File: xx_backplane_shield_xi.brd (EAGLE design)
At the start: 80 x 82.5 mm, 25 parts

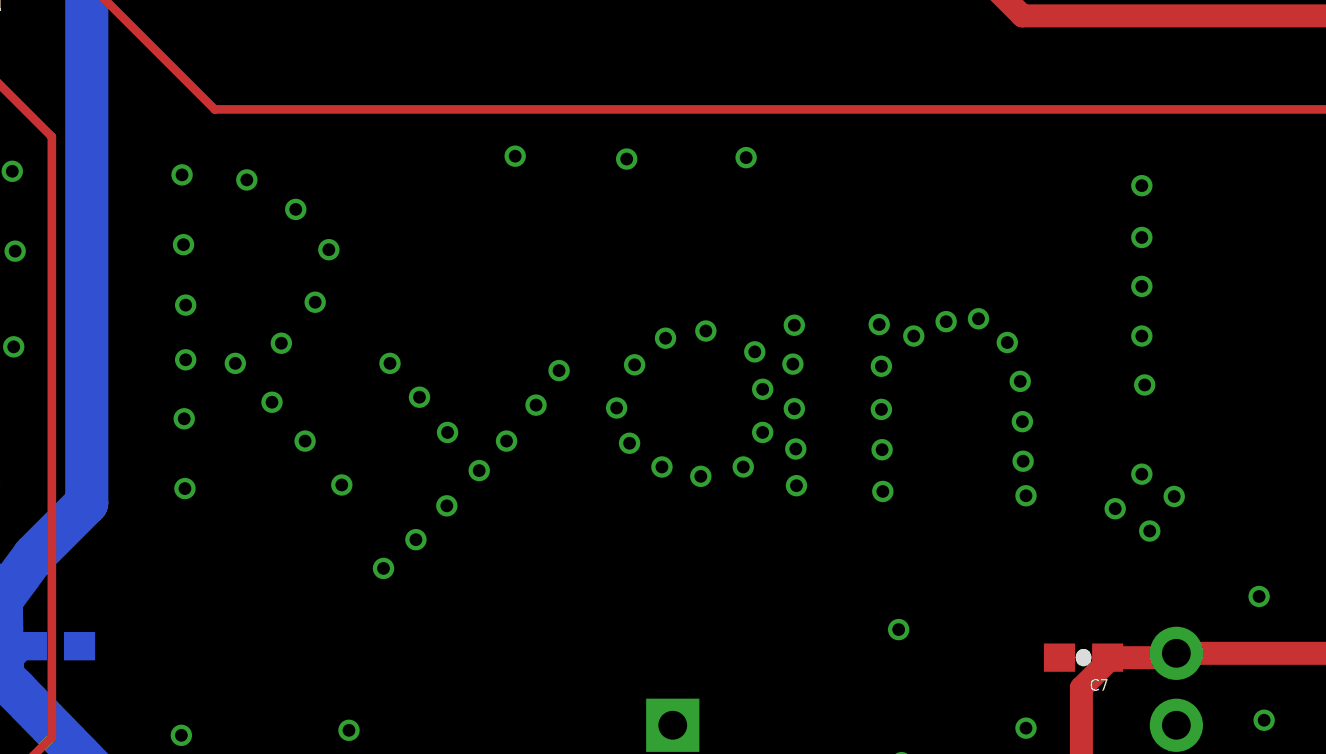
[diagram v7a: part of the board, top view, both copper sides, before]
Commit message: removing a few vias from my name
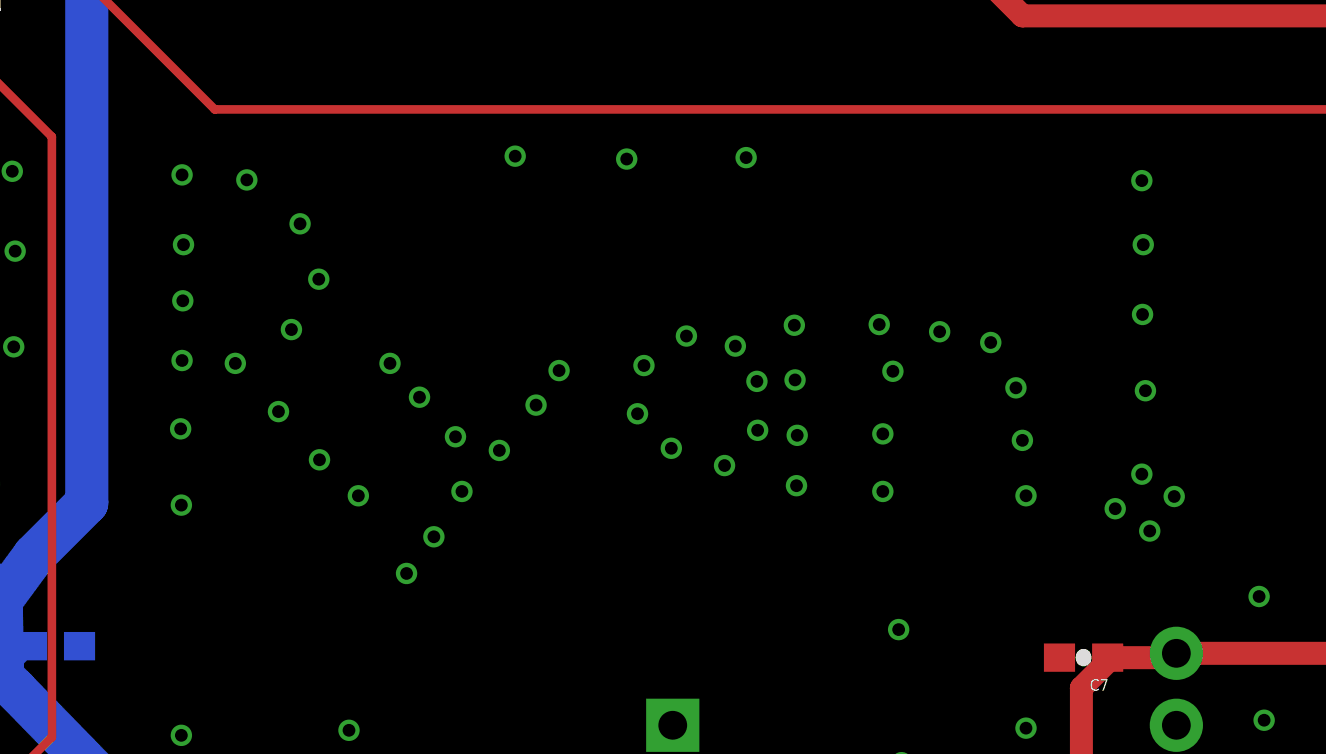
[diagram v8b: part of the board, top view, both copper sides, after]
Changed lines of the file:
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@@
 <via x="5.1562" y="56.4388" extent="1-16" drill="0.45"/>
 <via x="5.207" y="53.975" extent="1-16" drill="0.45"/>
-<via x="5.2832" y="51.8414" extent="1-16" drill="0.45"/>
-<via x="5.2832" y="49.911" extent="1-16" drill="0.45"/>
-<via x="5.2324" y="47.8282" extent="1-16" drill="0.45"/>
-<via x="5.2578" y="45.3644" extent="1-16" drill="0.45"/>
+<via x="5.1816" y="51.9938" extent="1-16" drill="0.45"/>
+<via x="5.1562" y="49.8856" extent="1-16" drill="0.45"/>
+<via x="5.1054" y="47.4726" extent="1-16" drill="0.45"/>
+<via x="5.1308" y="44.7802" extent="1-16" drill="0.45"/>
 <via x="7.4422" y="56.261" extent="1-16" drill="0.45"/>
-<via x="9.1694" y="55.2196" extent="1-16" drill="0.45"/>
-<via x="10.3378" y="53.7972" extent="1-16" drill="0.45"/>
-<via x="9.8552" y="51.943" extent="1-16" drill="0.45"/>
-<via x="8.6614" y="50.4952" extent="1-16" drill="0.45"/>
+<via x="9.3218" y="54.7116" extent="1-16" drill="0.45"/>
+<via x="9.9822" y="52.7558" extent="1-16" drill="0.45"/>
+<via x="9.017" y="50.9778" extent="1-16" drill="0.45"/>
 <via x="7.0358" y="49.784" extent="1-16" drill="0.45"/>
-<via x="8.3312" y="48.4124" extent="1-16" drill="0.45"/>
-<via x="9.4996" y="47.0408" extent="1-16" drill="0.45"/>
-<via x="10.795" y="45.4914" extent="1-16" drill="0.45"/>
+<via x="8.5598" y="48.0822" extent="1-16" drill="0.45"/>
+<via x="10.0076" y="46.3804" extent="1-16" drill="0.45"/>
+<via x="11.3792" y="45.1104" extent="1-16" drill="0.45"/>
 <via x="12.4968" y="49.784" extent="1-16" drill="0.45"/>
 <via x="13.5382" y="48.5902" extent="1-16" drill="0.45"/>
-<via x="14.5288" y="47.3456" extent="1-16" drill="0.45"/>
-<via x="15.6464" y="45.9994" extent="1-16" drill="0.45"/>
-<via x="16.6116" y="47.0408" extent="1-16" drill="0.45"/>
+<via x="14.8082" y="47.1932" extent="1-16" drill="0.45"/>
+<via x="16.3576" y="46.7106" extent="1-16" drill="0.45"/>
 <via x="17.653" y="48.3108" extent="1-16" drill="0.45"/>
 <via x="18.4658" y="49.53" extent="1-16" drill="0.45"/>
-<via x="14.5034" y="44.7548" extent="1-16" drill="0.45"/>
-<via x="13.4112" y="43.561" extent="1-16" drill="0.45"/>
-<via x="12.2682" y="42.545" extent="1-16" drill="0.45"/>
-<via x="25.654" y="48.8696" extent="1-16" drill="0.45"/>
-<via x="25.3746" y="50.1904" extent="1-16" drill="0.45"/>
-<via x="23.6474" y="50.927" extent="1-16" drill="0.45"/>
-<via x="22.225" y="50.673" extent="1-16" drill="0.45"/>
-<via x="21.1328" y="49.7332" extent="1-16" drill="0.45"/>
-<via x="20.4978" y="48.2092" extent="1-16" drill="0.45"/>
-<via x="20.955" y="46.9646" extent="1-16" drill="0.45"/>
-<via x="22.098" y="46.1264" extent="1-16" drill="0.45"/>
-<via x="23.4696" y="45.7962" extent="1-16" drill="0.45"/>
-<via x="24.9682" y="46.1264" extent="1-16" drill="0.45"/>
-<via x="25.654" y="47.3456" extent="1-16" drill="0.45"/>
-<via x="26.7716" y="48.1838" extent="1-16" drill="0.45"/>
+<via x="15.0368" y="45.2628" extent="1-16" drill="0.45"/>
+<via x="14.0462" y="43.6626" extent="1-16" drill="0.45"/>
+<via x="13.081" y="42.3672" extent="1-16" drill="0.45"/>
+<via x="25.4508" y="49.149" extent="1-16" drill="0.45"/>
+<via x="24.6888" y="50.3936" extent="1-16" drill="0.45"/>
+<via x="22.9616" y="50.7492" extent="1-16" drill="0.45"/>
+<via x="21.463" y="49.7078" extent="1-16" drill="0.45"/>
+<via x="21.2344" y="48.006" extent="1-16" drill="0.45"/>
+<via x="22.4282" y="46.7868" extent="1-16" drill="0.45"/>
+<via x="24.3078" y="46.1772" extent="1-16" drill="0.45"/>
+<via x="25.4762" y="47.4218" extent="1-16" drill="0.45"/>
 <via x="26.7716" y="51.1302" extent="1-16" drill="0.45"/>
 <via x="29.8958" y="45.2628" extent="1-16" drill="0.45"/>
-<via x="26.8224" y="46.7614" extent="1-16" drill="0.45"/>
+<via x="26.8732" y="47.244" extent="1-16" drill="0.45"/>
 <via x="26.8478" y="45.466" extent="1-16" drill="0.45"/>
-<via x="26.7208" y="49.7586" extent="1-16" drill="0.45"/>
-<via x="29.8704" y="46.736" extent="1-16" drill="0.45"/>
-<via x="29.845" y="48.1584" extent="1-16" drill="0.45"/>
-<via x="29.845" y="49.6824" extent="1-16" drill="0.45"/>
+<via x="26.797" y="49.1998" extent="1-16" drill="0.45"/>
+<via x="29.8958" y="47.2948" extent="1-16" drill="0.45"/>
 <via x="29.7688" y="51.1556" extent="1-16" drill="0.45"/>
-<via x="30.988" y="50.7492" extent="1-16" drill="0.45"/>
-<via x="32.131" y="51.2572" extent="1-16" drill="0.45"/>
-<via x="33.274" y="51.3588" extent="1-16" drill="0.45"/>
-<via x="34.29" y="50.5206" extent="1-16" drill="0.45"/>
-<via x="34.7472" y="49.149" extent="1-16" drill="0.45"/>
-<via x="34.8234" y="47.7266" extent="1-16" drill="0.45"/>
-<via x="34.8488" y="46.3296" extent="1-16" drill="0.45"/>
+<via x="30.2514" y="49.5046" extent="1-16" drill="0.45"/>
+<via x="31.9024" y="50.9016" extent="1-16" drill="0.45"/>
+<via x="33.7058" y="50.5206" extent="1-16" drill="0.45"/>
+<via x="34.5948" y="48.9204" extent="1-16" drill="0.45"/>
+<via x="34.8234" y="47.0662" extent="1-16" drill="0.45"/>
 <via x="34.9504" y="45.1104" extent="1-16" drill="0.45"/>
-<via x="39.0398" y="56.0578" extent="1-16" drill="0.45"/>
-<via x="39.0398" y="54.229" extent="1-16" drill="0.45"/>
-<via x="39.0398" y="52.5018" extent="1-16" drill="0.45"/>
-<via x="39.0398" y="50.7492" extent="1-16" drill="0.45"/>
-<via x="39.1414" y="49.022" extent="1-16" drill="0.45"/>
+<via x="39.0398" y="56.2356" extent="1-16" drill="0.45"/>
+<via x="39.0906" y="53.975" extent="1-16" drill="0.45"/>
+<via x="39.0652" y="51.5112" extent="1-16" drill="0.45"/>
+<via x="39.1668" y="48.8188" extent="1-16" drill="0.45"/>
+<wire x1="39.1414" y1="49.022" x2="39.1414" y2="49.022" width="0" layer="19" extent="1-16"/>
 <via x="39.0398" y="45.8724" extent="1-16" drill="0.45"/>
 <via x="38.1" y="44.6532" extent="1-16" drill="0.45"/>
